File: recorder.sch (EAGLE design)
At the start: 45 parts, among them M1 ELECTRET_MICROPHON-WM-61A, Q1 4.096MHz, T1 MMBT3904 NPN, U1 ISD15100

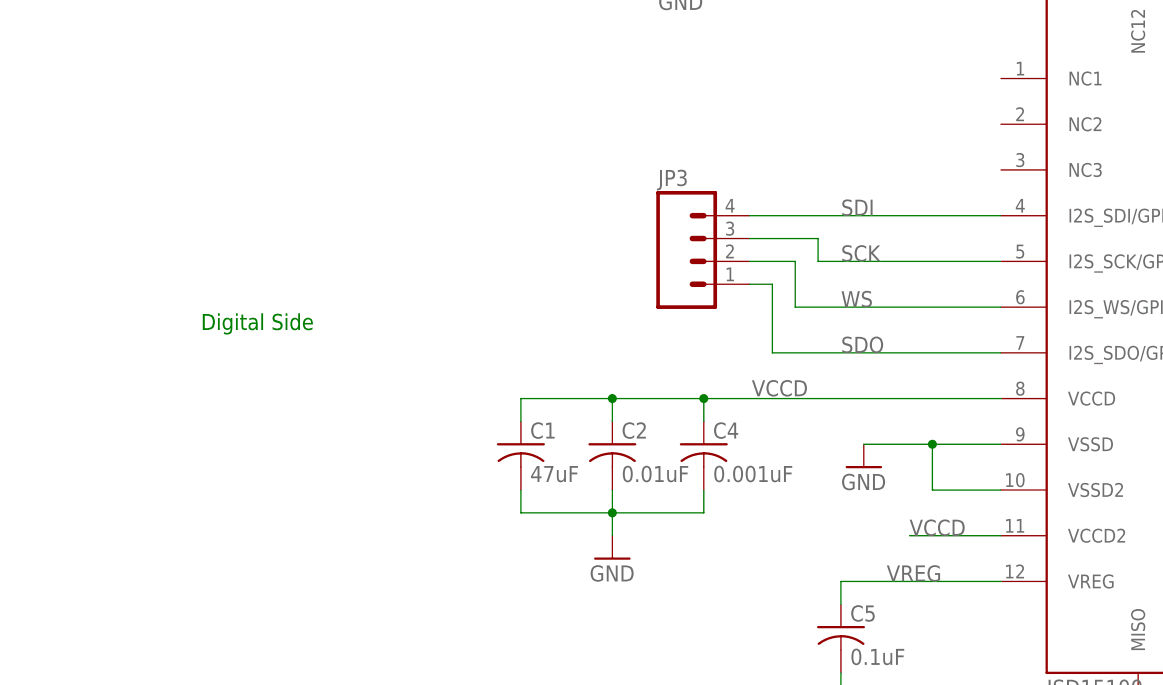
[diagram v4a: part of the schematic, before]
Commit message: spaced out component further for easier routing and to pass Sunstone DRC rules. Also, added VCC, GND 2-pin connector
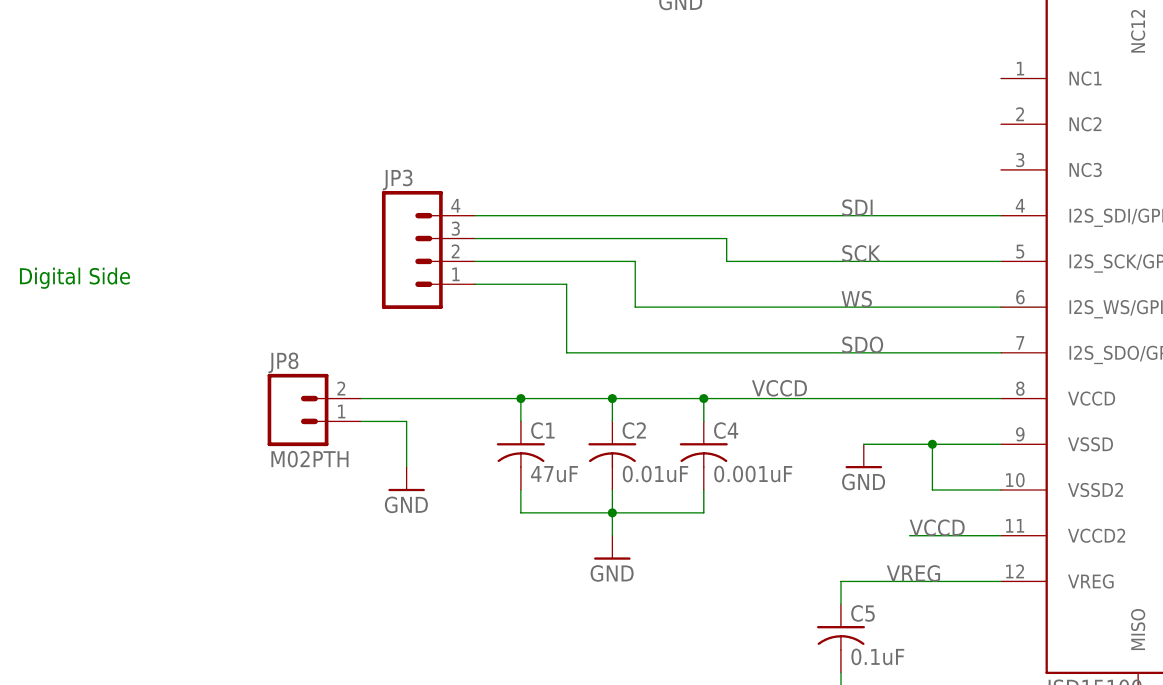
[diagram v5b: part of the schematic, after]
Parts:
- added JP8: M02PTH, SparkFun-Connectors:M02PTH
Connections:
- net GND: now also JP8.1
- net VCCD: now also JP8.2
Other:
- moved on the sheet: JP3
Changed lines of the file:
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@@
 <part name="Q1" library="adafruit" deviceset="CRYSTAL" device="SM49" value="4.096MHz"/>
 <part name="JP4" library="SparkFun-Connectors" deviceset="AUDIO-JACK" device="SMD2"/>
-<part name="JP3" library="SparkFun-Connectors" deviceset="M04" device="PTH"/>
 <part name="JP5" library="SparkFun-Connectors" deviceset="M04" device="PTH"/>
 <part name="JP2" library="SparkFun-Connectors" deviceset="M04" device="PTH"/>
@@
 <part name="GND15" library="SparkFun-Aesthetics" deviceset="GND" device=""/>
 <part name="GND16" library="SparkFun-Aesthetics" deviceset="GND" device=""/>
+<part name="GND17" library="SparkFun-Aesthetics" deviceset="GND" device=""/>
+<part name="JP3" library="SparkFun-Connectors" deviceset="M04" device="PTH"/>
+<part name="JP8" library="SparkFun-Connectors" deviceset="M02" device="PTH"/>
 </parts>
 <sheets>
@@
 <text x="-73.66" y="25.4" size="1.778" layer="91">SPI Connections</text>
 <text x="106.68" y="223.52" size="1.778" layer="91">Is this redundant if we have a headphone jack? Should speaker be off-board or mounted to PCB?</text>
-<text x="-101.6" y="81.28" size="1.778" layer="91">Digital Side</text>
+<text x="-121.92" y="86.36" size="1.778" layer="91">Digital Side</text>
 <text x="30.48" y="-7.62" size="1.778" layer="91">Digital</text>
 <text x="193.04" y="88.9" size="1.778" layer="91">Digital</text>
@@
 <instance part="Q1" gate="G$1" x="119.38" y="91.44"/>
 <instance part="JP4" gate="G$1" x="33.02" y="15.24" rot="R90"/>
-<instance part="JP3" gate="G$1" x="-45.72" y="88.9"/>
 <instance part="JP5" gate="G$1" x="104.14" y="127" rot="R180"/>
 <instance part="JP2" gate="G$1" x="-68.58" y="12.7"/>
@@
 <instance part="GND15" gate="1" x="149.86" y="73.66"/>
 <instance part="GND16" gate="1" x="33.02" y="30.48"/>
+<instance part="GND17" gate="1" x="-78.74" y="63.5"/>
+<instance part="JP3" gate="G$1" x="-76.2" y="88.9"/>
+<instance part="JP8" gate="G$1" x="-91.44" y="71.12"/>
 </instances>
 <busses>
@@
 <segment>
 <pinref part="U1" gate="G$1" pin="VCCD"/>
-<pinref part="C1" gate="G$1" pin="1"/>
 <wire x1="-12.7" y1="73.66" x2="-45.72" y2="73.66" width="0.1524" layer="91"/>
 <wire x1="-45.72" y1="73.66" x2="-55.88" y2="73.66" width="0.1524" layer="91"/>
-<wire x1="-55.88" y1="73.66" x2="-66.04" y2="73.66" width="0.1524" layer="91"/>
-<wire x1="-66.04" y1="73.66" x2="-66.04" y2="71.12" width="0.1524" layer="91"/>
 <pinref part="C2" gate="G$1" pin="1"/>
 <wire x1="-55.88" y1="71.12" x2="-55.88" y2="73.66" width="0.1524" layer="91"/>
@@
 <wire x1="-45.72" y1="71.12" x2="-45.72" y2="73.66" width="0.1524" layer="91"/>
 <label x="-40.386" y="73.914" size="1.778" layer="95"/>
+<junction x="-45.72" y="73.66"/>
+<pinref part="C1" gate="G$1" pin="1"/>
+<wire x1="-66.04" y1="73.66" x2="-66.04" y2="71.12" width="0.1524" layer="91"/>
+<pinref part="JP8" gate="G$1" pin="2"/>
+<wire x1="-66.04" y1="73.66" x2="-83.82" y2="73.66" width="0.1524" layer="91"/>
+<wire x1="-66.04" y1="73.66" x2="-55.88" y2="73.66" width="0.1524" layer="91"/>
+<junction x="-66.04" y="73.66"/>
 <junction x="-55.88" y="73.66"/>
-<junction x="-45.72" y="73.66"/>
 </segment>
 </net>
@@
 <segment>
 <pinref part="U1" gate="G$1" pin="I2S_SDI/GPIO7"/>
-<wire x1="-40.64" y1="93.98" x2="-12.7" y2="93.98" width="0.1524" layer="91"/>
 <label x="-30.48" y="93.98" size="1.778" layer="95"/>
+<wire x1="-12.7" y1="93.98" x2="-71.12" y2="93.98" width="0.1524" layer="91"/>
 <pinref part="JP3" gate="G$1" pin="4"/>
 </segment>
@@
 <net name="SCK" class="0">
 <segment>
-<wire x1="-40.64" y1="91.44" x2="-33.02" y2="91.44" width="0.1524" layer="91"/>
-<wire x1="-33.02" y1="91.44" x2="-33.02" y2="88.9" width="0.1524" layer="91"/>
+<wire x1="-43.18" y1="91.44" x2="-43.18" y2="88.9" width="0.1524" layer="91"/>
 <pinref part="U1" gate="G$1" pin="I2S_SCK/GPIO6"/>
-<wire x1="-33.02" y1="88.9" x2="-12.7" y2="88.9" width="0.1524" layer="91"/>
+<wire x1="-43.18" y1="88.9" x2="-12.7" y2="88.9" width="0.1524" layer="91"/>
 <label x="-30.48" y="88.9" size="1.778" layer="95"/>
+<wire x1="-43.18" y1="91.44" x2="-71.12" y2="91.44" width="0.1524" layer="91"/>
 <pinref part="JP3" gate="G$1" pin="3"/>
 </segment>
@@
 <net name="WS" class="0">
 <segment>
-<wire x1="-40.64" y1="88.9" x2="-35.56" y2="88.9" width="0.1524" layer="91"/>
-<wire x1="-35.56" y1="88.9" x2="-35.56" y2="83.82" width="0.1524" layer="91"/>
+<wire x1="-53.34" y1="88.9" x2="-53.34" y2="83.82" width="0.1524" layer="91"/>
 <pinref part="U1" gate="G$1" pin="I2S_WS/GPIO5"/>
-<wire x1="-35.56" y1="83.82" x2="-12.7" y2="83.82" width="0.1524" layer="91"/>
+<wire x1="-53.34" y1="83.82" x2="-12.7" y2="83.82" width="0.1524" layer="91"/>
 <label x="-30.48" y="83.82" size="1.778" layer="95"/>
+<wire x1="-53.34" y1="88.9" x2="-71.12" y2="88.9" width="0.1524" layer="91"/>
 <pinref part="JP3" gate="G$1" pin="2"/>
 </segment>
@@
 <net name="SDO" class="0">
 <segment>
-<wire x1="-40.64" y1="86.36" x2="-38.1" y2="86.36" width="0.1524" layer="91"/>
-<wire x1="-38.1" y1="86.36" x2="-38.1" y2="78.74" width="0.1524" layer="91"/>
+<wire x1="-60.96" y1="86.36" x2="-60.96" y2="78.74" width="0.1524" layer="91"/>
 <pinref part="U1" gate="G$1" pin="I2S_SDO/GPIO4"/>
-<wire x1="-38.1" y1="78.74" x2="-12.7" y2="78.74" width="0.1524" layer="91"/>
+<wire x1="-60.96" y1="78.74" x2="-12.7" y2="78.74" width="0.1524" layer="91"/>
 <label x="-30.48" y="78.74" size="1.778" layer="95"/>
+<wire x1="-60.96" y1="86.36" x2="-71.12" y2="86.36" width="0.1524" layer="91"/>
 <pinref part="JP3" gate="G$1" pin="1"/>
 </segment>
@@
 <pinref part="GND16" gate="1" pin="GND"/>
 </segment>
-</net>
+<segment>
+<pinref part="JP8" gate="G$1" pin="1"/>
+<pinref part="GND17" gate="1" pin="GND"/>
+<wire x1="-83.82" y1="71.12" x2="-78.74" y2="71.12" width="0.1524" layer="91"/>
+<wire x1="-78.74" y1="71.12" x2="-78.74" y2="66.04" width="0.1524" layer="91"/>
+</segment>
+</net>

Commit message: added design parameters readMe, BoM, changed C1 package to 1206
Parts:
- C1: device rcl:C-USC0402 -> rcl:C-USC1206
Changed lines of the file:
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@@
 <part name="C18" library="rcl" deviceset="C-US" device="C0402" value="27pF"/>
 <part name="C8" library="rcl" deviceset="C-US" device="C0402" value="0.1uF"/>
-<part name="C1" library="rcl" deviceset="C-US" device="C0402" value="47uF"/>
 <part name="C2" library="rcl" deviceset="C-US" device="C0402" value="0.01uF"/>
 <part name="C4" library="rcl" deviceset="C-US" device="C0402" value="0.001uF"/>
@@
 <part name="JP3" library="SparkFun-Connectors" deviceset="M04" device="PTH"/>
 <part name="JP8" library="SparkFun-Connectors" deviceset="M02" device="PTH"/>
+<part name="C1" library="rcl" deviceset="C-US" device="C1206" value="47uF"/>
 </parts>
 <sheets>
@@
 <instance part="C18" gate="G$1" x="129.54" y="83.82"/>
 <instance part="C8" gate="G$1" x="12.7" y="182.88" rot="R180"/>
-<instance part="C1" gate="G$1" x="-66.04" y="68.58"/>
 <instance part="C2" gate="G$1" x="-55.88" y="68.58"/>
 <instance part="C4" gate="G$1" x="-45.72" y="68.58"/>
@@
 <instance part="JP3" gate="G$1" x="-76.2" y="88.9"/>
 <instance part="JP8" gate="G$1" x="-91.44" y="71.12"/>
+<instance part="C1" gate="G$1" x="-66.04" y="68.58"/>
 </instances>
 <busses>
@@
 <label x="-40.386" y="73.914" size="1.778" layer="95"/>
 <junction x="-45.72" y="73.66"/>
-<pinref part="C1" gate="G$1" pin="1"/>
 <wire x1="-66.04" y1="73.66" x2="-66.04" y2="71.12" width="0.1524" layer="91"/>
 <pinref part="JP8" gate="G$1" pin="2"/>
@@
 <junction x="-66.04" y="73.66"/>
 <junction x="-55.88" y="73.66"/>
+<pinref part="C1" gate="G$1" pin="1"/>
 </segment>
 </net>
@@
 <pinref part="C2" gate="G$1" pin="2"/>
 <wire x1="-55.88" y1="58.42" x2="-55.88" y2="60.96" width="0.1524" layer="91"/>
-<pinref part="C1" gate="G$1" pin="2"/>
 <wire x1="-55.88" y1="60.96" x2="-55.88" y2="63.5" width="0.1524" layer="91"/>
 <wire x1="-66.04" y1="63.5" x2="-66.04" y2="60.96" width="0.1524" layer="91"/>
@@
 <junction x="-55.88" y="60.96"/>
 <pinref part="GND7" gate="1" pin="GND"/>
-</segment>
-<segment>
+<pinref part="C1" gate="G$1" pin="2"/>
+</segment>
+<segment>
